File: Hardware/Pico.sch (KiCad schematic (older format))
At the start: 5 parts, among them J2 1x3 picoblade, J3 1x3 picoblade, J4 1x2 picoblade, U1 Pico

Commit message: Add 2nd pyro, smd headers
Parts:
- added D2: LED red, LED_SMD:LED_0603_1608Metric, symbol Device:LED
- added D4: LED, LED_SMD:LED_0603_1608Metric, symbol Device:LED
- added R14, R15: 220, Resistor_SMD:R_0603_1608Metric, symbol Device:R
- U1: footprint RocketBrain:RPi_Pico_HAT -> RocketBrain:RPi_Pico_HAT_smd
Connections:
- net GND: now also R14.2, R15.2
- net buzz: now also U1.29 (GPIO22); no longer U1.9 (GPIO6)
- net boot: now reaches U1.10 (GPIO7)
- net boot: now also D2.1 (K)
- new net: D4.2 (A), R15.1
- new net: D2.2 (A), R14.1
- new net ready: D4.1 (K), U1.9 (GPIO6)
- no-connect marks 19 -> 17
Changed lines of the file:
@@
 F 0 "U1" H 5650 4940 50  0000 C CNN
 F 1 "Pico" H 5650 4849 50  0000 C CNN
-F 2 "RocketBrain:RPi_Pico_HAT" V 7425 5400 50  0001 C CNN
+F 2 "RocketBrain:RPi_Pico_HAT_smd" V 7425 5400 50  0001 C CNN
 F 3 "" H 7425 5400 50  0001 C CNN
 	1    5650 3725
@@
 Wire Wire Line
 	4650 5700 4925 5700
-Text Label 4775 3575 2    50   ~ 0
+Text Label 6575 3875 0    50   ~ 0
 buzz
 Wire Wire Line
@@
 	4400 4475 4400 3975
 NoConn ~ 4950 4675
-NoConn ~ 4950 3675
 NoConn ~ 4950 2875
 NoConn ~ 4950 2775
@@
 Wire Wire Line
 	6350 3175 7025 3175
-NoConn ~ 6350 3875
+$Comp
+L Device:LED D4
+U 1 1 6115C3C5
+P 3350 4500
+F 0 "D4" V 3297 4580 50  0000 L CNN
+F 1 "LED " V 3388 4580 50  0000 L CNN
+F 2 "LED_SMD:LED_0603_1608Metric" H 3350 4500 50  0001 C CNN
+F 3 "~" H 3350 4500 50  0001 C CNN
+	1    3350 4500
+	0    1    1    0
+$EndComp
+$Comp
+L Device:LED D2
+U 1 1 6115C9D0
+P 2950 4500
+F 0 "D2" V 2897 4580 50  0000 L CNN
+F 1 "LED red " V 3050 4500 50  0000 L CNN
+F 2 "LED_SMD:LED_0603_1608Metric" H 2950 4500 50  0001 C CNN
+F 3 "~" H 2950 4500 50  0001 C CNN
+	1    2950 4500
+	0    1    1    0
+$EndComp
+$Comp
+L Device:R R14
+U 1 1 6115DA62
+P 2950 4875
+F 0 "R14" H 3020 4921 50  0000 L CNN
+F 1 "220" H 3020 4830 50  0000 L CNN
+F 2 "Resistor_SMD:R_0603_1608Metric" V 2880 4875 50  0001 C CNN
+F 3 "~" H 2950 4875 50  0001 C CNN
+	1    2950 4875
+	1    0    0    -1
+$EndComp
+$Comp
+L Device:R R15
+U 1 1 6115E36E
+P 3350 4875
+F 0 "R15" H 3420 4921 50  0000 L CNN
+F 1 "220" H 3420 4830 50  0000 L CNN
+F 2 "Resistor_SMD:R_0603_1608Metric" V 3280 4875 50  0001 C CNN
+F 3 "~" H 3350 4875 50  0001 C CNN
+	1    3350 4875
+	1    0    0    -1
+$EndComp
+Wire Wire Line
+	2950 4725 2950 4650
+Wire Wire Line
+	3350 4725 3350 4650
+$Comp
+L power:GND #PWR0119
+U 1 1 6116046B
+P 3150 5125
+F 0 "#PWR0119" H 3150 4875 50  0001 C CNN
+F 1 "GND" H 3155 4952 50  0000 C CNN
+F 2 "" H 3150 5125 50  0001 C CNN
+F 3 "" H 3150 5125 50  0001 C CNN
+	1    3150 5125
+	1    0    0    -1
+$EndComp
+Wire Wire Line
+	2950 5025 2950 5075
+Wire Wire Line
+	2950 5075 3150 5075
+Wire Wire Line
+	3350 5075 3350 5025
+Wire Wire Line
+	3150 5075 3150 5125
+Connection ~ 3150 5075
+Wire Wire Line
+	3150 5075 3350 5075
+Text Label 2950 4225 1    50   ~ 0
+boot
+Wire Wire Line
+	2950 4225 2950 4350
+Text Label 3350 4225 1    50   ~ 0
+ready
+Wire Wire Line
+	3350 4225 3350 4350
+Text Label 4775 3675 2    50   ~ 0
+boot
+Wire Wire Line
+	4775 3675 4950 3675
+Text Label 4775 3575 2    50   ~ 0
+ready
+Wire Wire Line
+	6575 3875 6350 3875
 $EndSCHEMATC

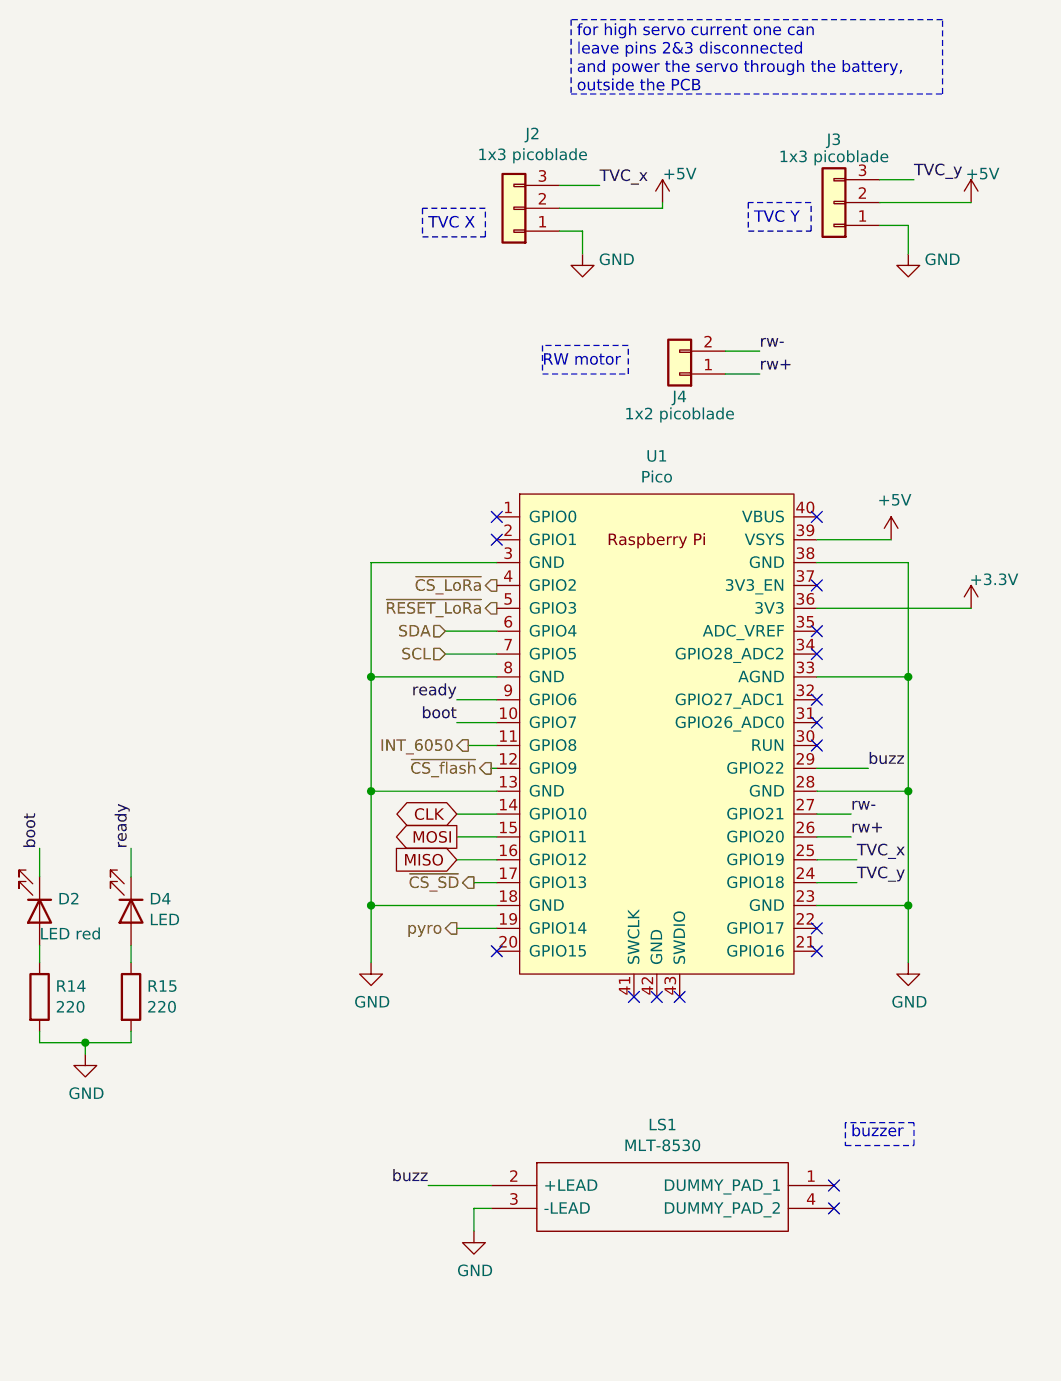
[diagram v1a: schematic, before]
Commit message: Update schematic, component placement
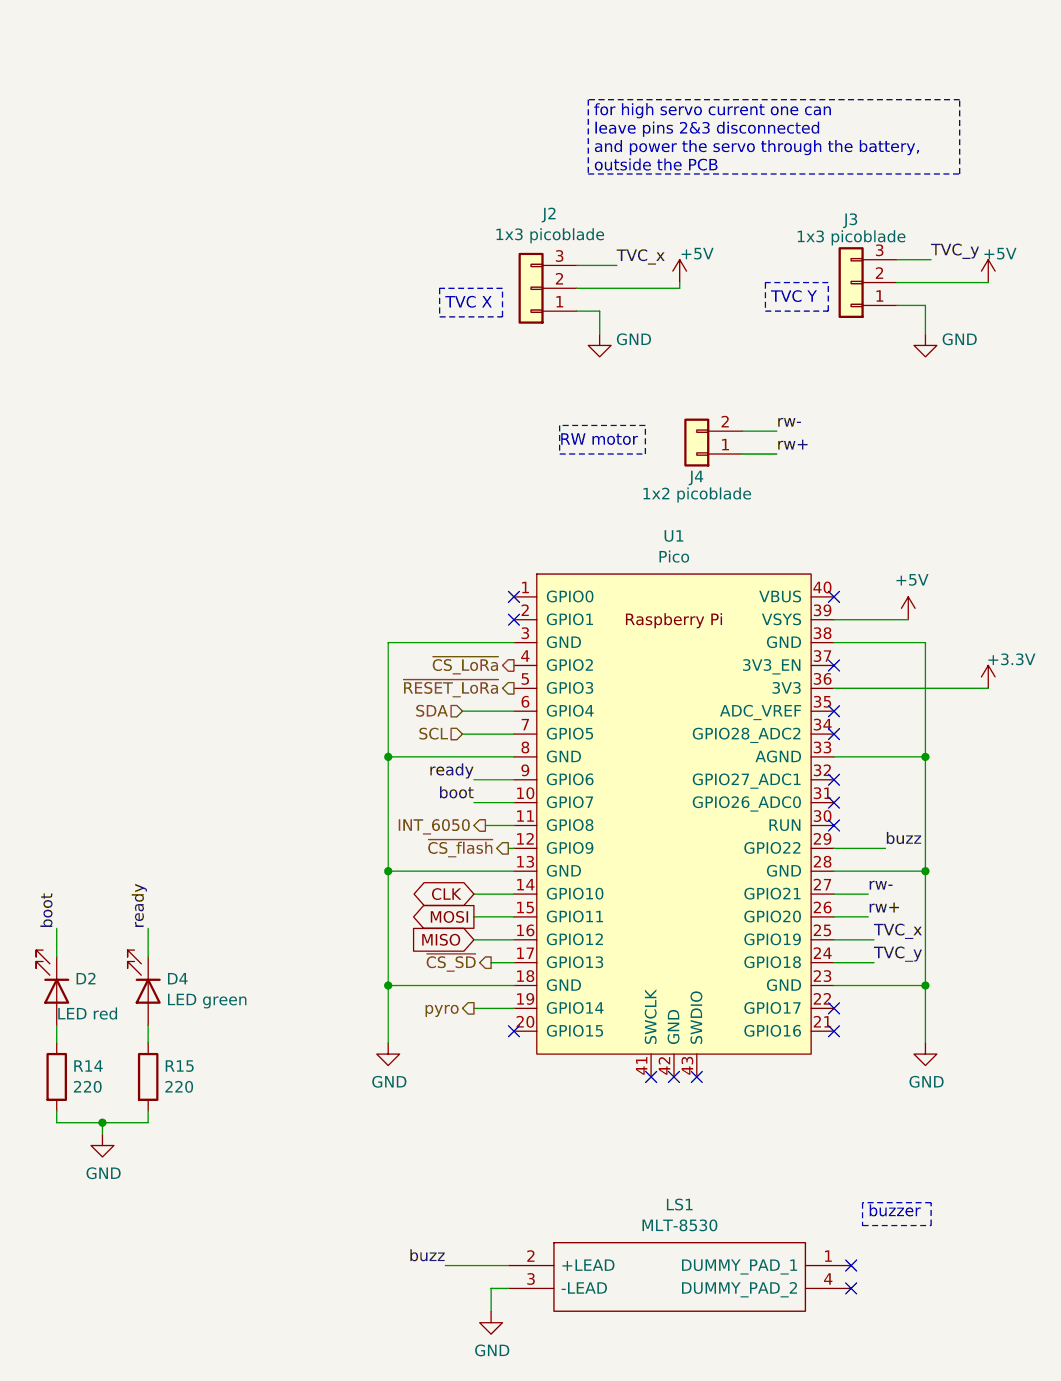
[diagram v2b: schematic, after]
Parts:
- D4: value LED -> LED green
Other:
- moved on the sheet: D2, D4, J2, J3, J4, LS1, R14, R15, U1

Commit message: Update schematic and routing
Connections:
- net INT_6050: now also U1.2 (GPIO1); no longer U1.11 (GPIO8)
- net ready: now also U1.1 (GPIO0); no longer U1.9 (GPIO6)
- net ~CS_LoRa: now also U1.20 (GPIO15); no longer U1.4 (GPIO2)
- net pyro2: now reaches U1.32 (GPIO27_ADC1)
- net pyro1: now reaches U1.34 (GPIO28_ADC2)
- net pyro: no longer names the net of U1.19 (GPIO14)
- no-connect marks 17 -> 15
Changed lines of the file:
@@
 buzz
 Wire Wire Line
-	4850 3925 5025 3925
+	4850 3125 5025 3125
 Wire Wire Line
 	4850 4525 5025 4525
@@
 	-1   0    0    1
 $EndComp
-Text HLabel 4850 4925 0    50   Output ~ 0
-pyro
-Wire Wire Line
-	4850 4925 5025 4925
-Text HLabel 5025 3425 0    50   Output ~ 0
+Text HLabel 6550 3725 2    50   Output ~ 0
+pyro1
+Text HLabel 4875 5025 0    50   Output ~ 0
 ~CS_LoRa
 Text HLabel 5025 3525 0    50   Output ~ 0
@@
 Wire Wire Line
 	4475 4825 4475 4325
-NoConn ~ 5025 5025
-NoConn ~ 5025 3225
-NoConn ~ 5025 3125
 NoConn ~ 6425 3125
 NoConn ~ 6425 3425
 NoConn ~ 6425 3625
-NoConn ~ 6425 3725
-NoConn ~ 6425 3925
 NoConn ~ 6425 4025
 NoConn ~ 6425 4125
 NoConn ~ 6425 4925
 NoConn ~ 6425 5025
-Text HLabel 4900 4125 0    50   Output ~ 0
+Text HLabel 4925 3225 0    50   Output ~ 0
 INT_6050
 Wire Wire Line
@@
 Wire Wire Line
 	4850 4025 5025 4025
-Text Label 4850 3925 2    50   ~ 0
+Text Label 4850 3125 2    50   ~ 0
 ready
 Wire Wire Line
 	6650 4225 6425 4225
+Wire Wire Line
+	4875 5025 5025 5025
+NoConn ~ 5025 3425
+Wire Wire Line
+	6425 3725 6550 3725
+Text HLabel 6550 3925 2    50   Output ~ 0
+pyro2
+Wire Wire Line
+	6550 3925 6425 3925
+NoConn ~ 5025 4925
+Wire Wire Line
+	4925 3225 5025 3225
+NoConn ~ 4900 4125
 $EndSCHEMATC

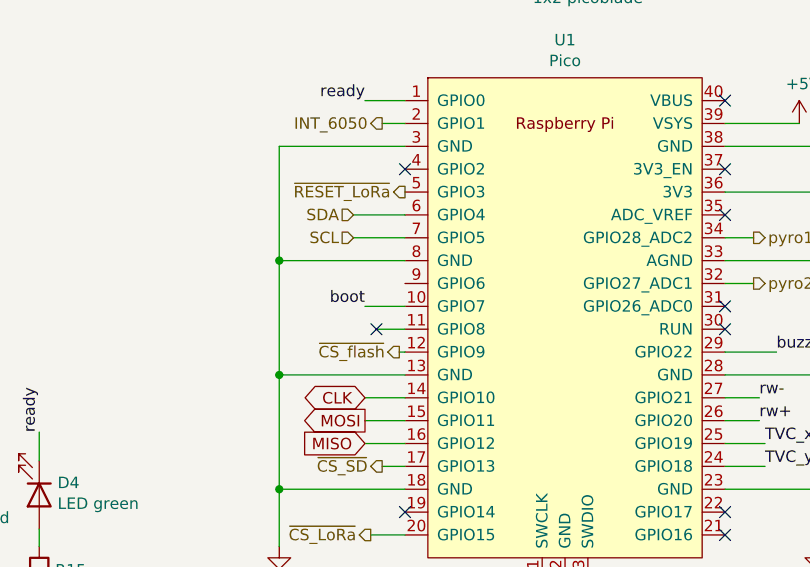
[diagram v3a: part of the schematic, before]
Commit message: Modify RPi Pico footprint, update routing
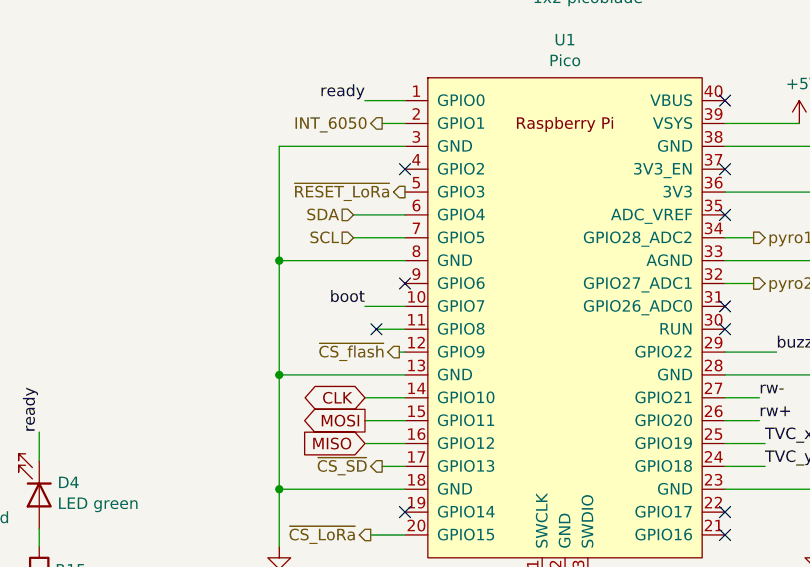
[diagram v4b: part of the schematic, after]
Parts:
- U1: footprint RocketBrain:RPi_Pico_HAT_smd -> RocketBrain:RPi_Pico_HAT_smd_mod
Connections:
- no-connect marks 15 -> 16
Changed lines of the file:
@@
 F 0 "U1" H 5725 5290 50  0000 C CNN
 F 1 "Pico" H 5725 5199 50  0000 C CNN
-F 2 "RocketBrain:RPi_Pico_HAT_smd" V 7500 5750 50  0001 C CNN
+F 2 "RocketBrain:RPi_Pico_HAT_smd_mod" V 7500 5750 50  0001 C CNN
 F 3 "" H 7500 5750 50  0001 C CNN
 	1    5725 4075
@@
 	4925 3225 5025 3225
 NoConn ~ 4900 4125
+NoConn ~ 5025 3925
 $EndSCHEMATC

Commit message: Update silkscreen
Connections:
- net pyro1: now also U1.31 (GPIO26_ADC0); no longer U1.34 (GPIO28_ADC2)
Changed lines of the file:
@@
 	-1   0    0    1
 $EndComp
-Text HLabel 6550 3725 2    50   Output ~ 0
+Text HLabel 6550 4025 2    50   Output ~ 0
 pyro1
 Text HLabel 4875 5025 0    50   Output ~ 0
@@
 NoConn ~ 6425 3425
 NoConn ~ 6425 3625
-NoConn ~ 6425 4025
 NoConn ~ 6425 4125
 NoConn ~ 6425 4925
@@
 	4875 5025 5025 5025
 NoConn ~ 5025 3425
-Wire Wire Line
-	6425 3725 6550 3725
 Text HLabel 6550 3925 2    50   Output ~ 0
 pyro2
@@
 NoConn ~ 4900 4125
 NoConn ~ 5025 3925
+Wire Wire Line
+	6550 4025 6425 4025
+NoConn ~ 6425 3725
 $EndSCHEMATC

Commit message: Change regulator diode footprint, update routing
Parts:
- LS1: MANUFACTURER (none) -> Jiangsu Huaneng Elec
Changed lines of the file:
@@
 F 6 "Jiangsu Huaneng Elec" H 6350 5750 50  0001 L CNN "Manufacturer_Name"
 F 7 "MLT-8530" H 6350 5650 50  0001 L CNN "Manufacturer_Part_Number"
+F 8 "Jiangsu Huaneng Elec" H 5000 6050 50  0001 C CNN "MANUFACTURER"
 	1    5000 6050
 	1    0    0    -1
